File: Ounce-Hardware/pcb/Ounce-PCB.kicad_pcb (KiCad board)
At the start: 2 copper layers, 135 x 61 mm, 5 parts, among them U1 RaspberryPi_Pico2_W, U2 RaspberryPi_Pico, U3 RaspberryPi_Pico, U4 RaspberryPi_Pico, U5 RaspberryPi_Pico

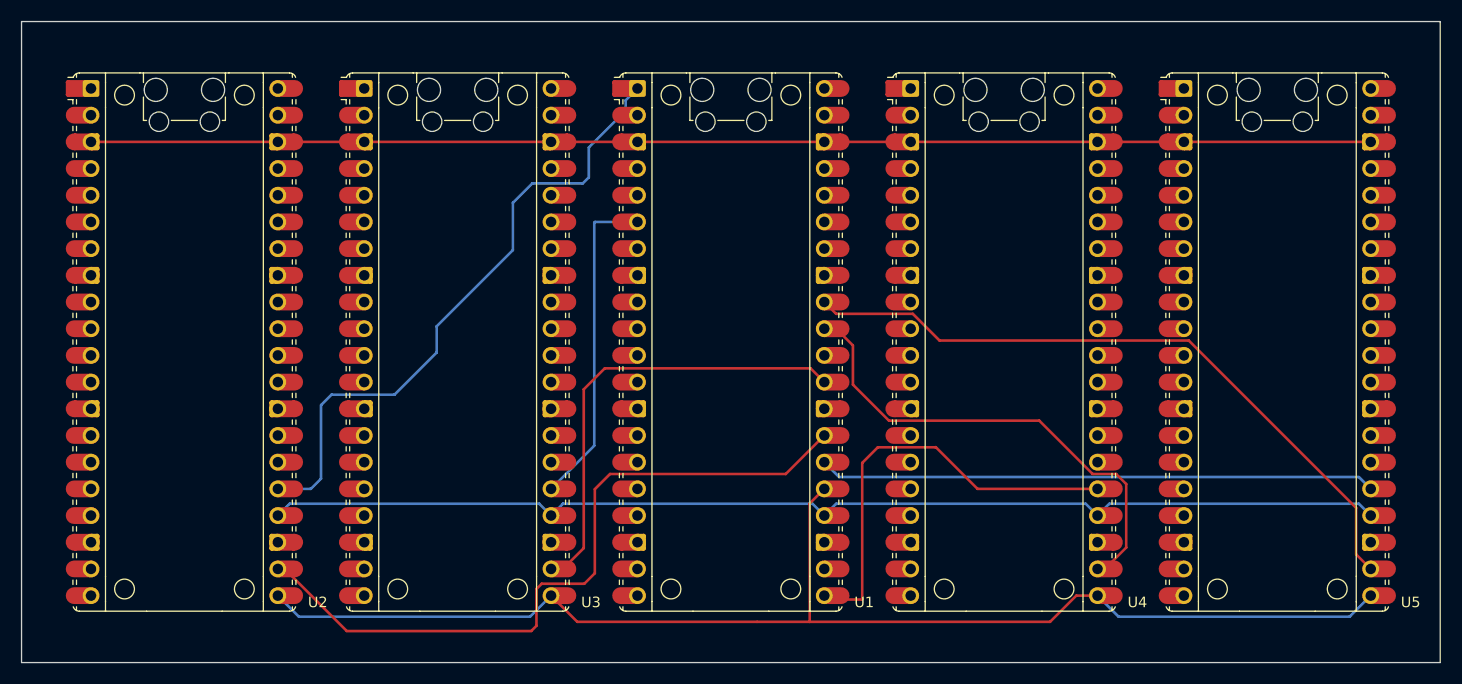
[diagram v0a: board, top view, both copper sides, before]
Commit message: Rotate U1 180 degrees and clear the routing
U1's USB now faces the opposite way to the four servants: rotated 180 degrees
in place at (150,100), still on F.Cu. All 103 track segments removed, so the
board is back to 25 ratlines with nothing routed.

I flipped it to the back first, which was the wrong reading of "flipped" -
that moved the module to B.Cu rather than turning it around. Undone.

The rotation moves U1's inner mounting pads from the top of the module to the
bottom, so the silkscreen no longer fits where it did: the servants are clear
below y=79.95 while U1 is only clear above y=120.05, leaving a common band of
79.95..120.05 instead of the 79.95..124.93 the text was spaced for. Four
silk_over_copper violations showed up where the rows clipped U1's pads.

Rows re-fitted into 81.0..119.0 with an exact 2.167mm gap between each. The
single letters drop from 9mm to 8mm high to make four rows fit that narrower
band without crowding; still the largest text on the board. No silkscreen
violations.

Ground is still restricted to pins 3 and 38.

Co-Authored-By: Claude Opus 5 <noreply@anthropic.com>
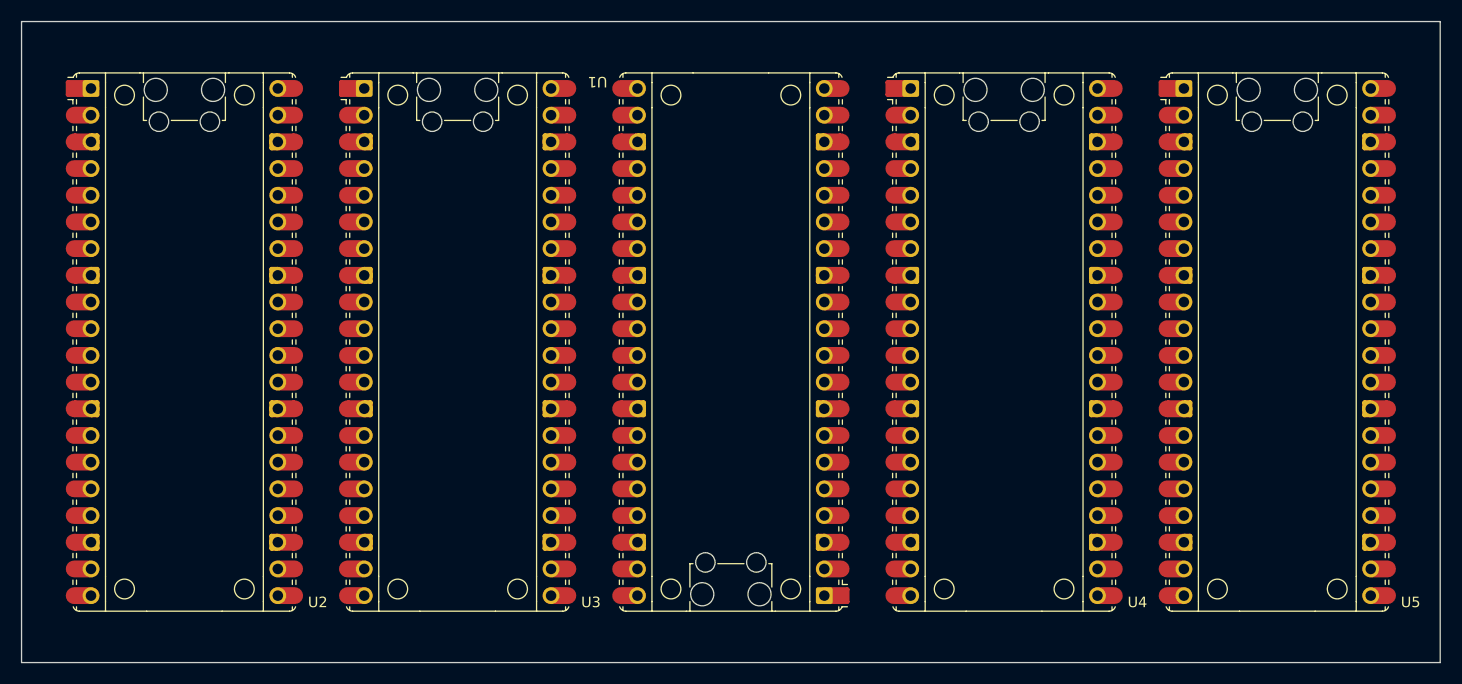
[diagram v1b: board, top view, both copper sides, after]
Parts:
- turned U1 to 180 degrees
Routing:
- net SPI0_MOSI: track 122.6 -> 0.00 mm
- net GND: track 121.8 -> 0.00 mm
- net SPI0_SCK: track 107.7 -> 0.00 mm
- net SPI0_CS0: track 68.9 -> 0.00 mm
- net SPI0_CS3: track 65.1 -> 0.00 mm
- net SPI0_MISO0: track 60.4 -> 0.00 mm
- net SPI0_MISO3: track 53.1 -> 0.00 mm
- net SPI0_CS2: track 46.7 -> 0.00 mm
- net SPI0_CS1: track 43.3 -> 0.00 mm
- net SPI0_MISO2: track 42.3 -> 0.00 mm
- net SPI0_MISO1: track 31.2 -> 0.00 mm

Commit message: Set the display silkscreen in Times New Roman, restore ground
The twelve display texts - OUNCE, THE, TITAN, SLAYER - now use Times New Roman
instead of KiCad's stroke font.

The credit stays in the stroke font, deliberately. At 2mm any TrueType serif
has hairline strokes below the silkscreen minimum, and DRC flags it: Times,
Georgia, Cambria and Palatino all failed at 2.4mm even in bold. It only passes
somewhere above 3.2mm, and by 3.4mm the text is 37.9 x 5.29mm, wider than the
corner allows and taller than the 5.17mm band between the last pad row and the
board edge. That leaves a window too narrow to build on, and hairlines dropping
out is a real silkscreen failure rather than a cosmetic one. The stroke font
has uniform thickness by design and is the right tool at that size.

Ground is restored, but not as it was: the 180 degree rotation moved U1's
ground pins from y=80.95 to y=119.05, so the old straight run no longer reaches
them. The chain now goes along the top through U2 and U3, down the 5mm channel
between U3 and U1 at x=137, across U1 at y=119.05, back up the channel between
U1 and U4 at x=163, then along the top through U4 and U5. Thirteen segments,
198mm, and DRC reports no unconnected ground.

The crossing at y=119.05 clears U1's mounting pads at y=120.05 by 0.88mm.

Co-Authored-By: Claude Opus 5 <noreply@anthropic.com>
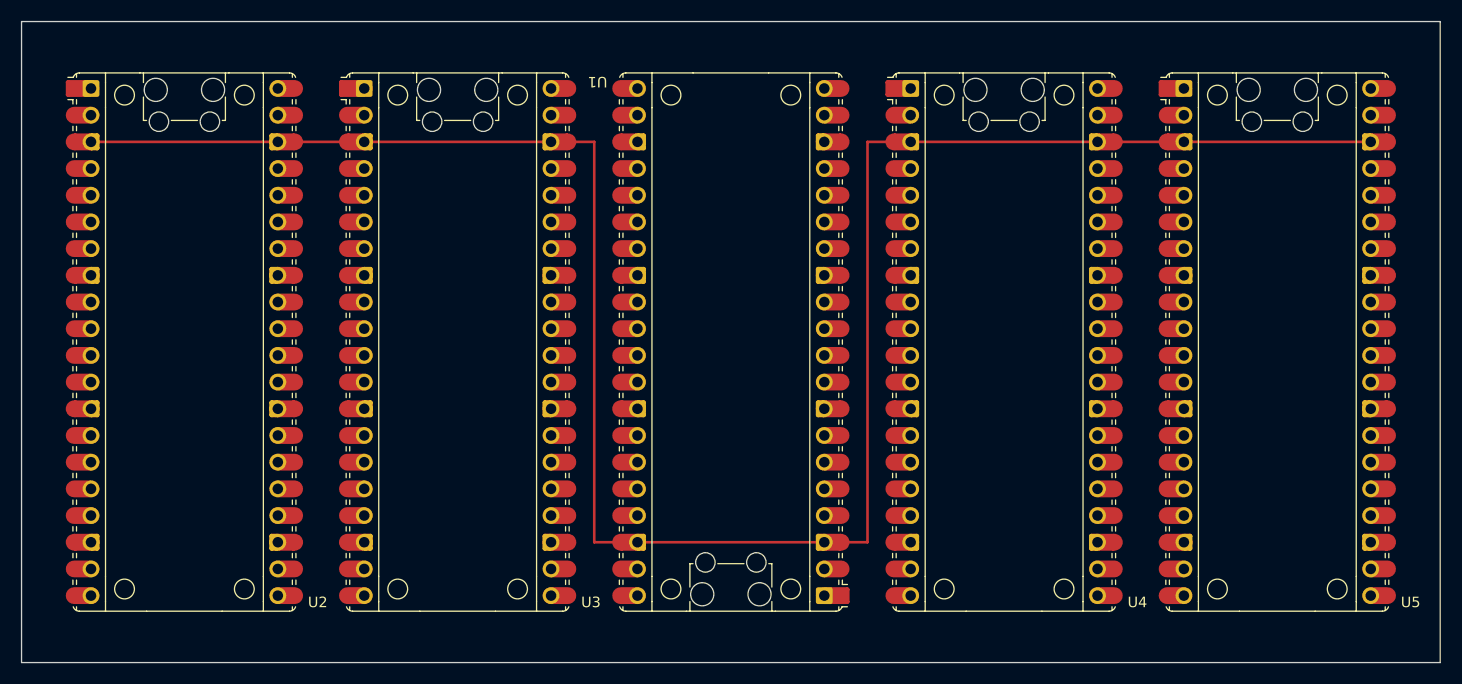
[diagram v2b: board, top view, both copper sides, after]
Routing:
- net GND: track 0.00 -> 198.0 mm
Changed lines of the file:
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@@
 		(effects
 			(font
+				(face "Times New Roman")
 				(size 5.5 2.1)
 				(thickness 0.8)
@@
 		(effects
 			(font
+				(face "Times New Roman")
 				(size 6 4)
 				(thickness 1)
@@
 		(effects
 			(font
+				(face "Times New Roman")
 				(size 8 6.2)
 				(thickness 1.1)
@@
 		(effects
 			(font
+				(face "Times New Roman")
 				(size 8 6.2)
 				(thickness 1.1)
@@
 		(effects
 			(font
+				(face "Times New Roman")
 				(size 8 6.2)
 				(thickness 1.1)
@@
 		(effects
 			(font
+				(face "Times New Roman")
 				(size 8 6.2)
 				(thickness 1.1)
@@
 		(effects
 			(font
+				(face "Times New Roman")
 				(size 8 6.2)
 				(thickness 1.1)
@@
 		(effects
 			(font
+				(face "Times New Roman")
 				(size 8 6.2)
 				(thickness 1.1)
@@
 		(effects
 			(font
+				(face "Times New Roman")
 				(size 8 6.2)
 				(thickness 1.1)
@@
 		(effects
 			(font
+				(face "Times New Roman")
 				(size 8 6.2)
 				(thickness 1.1)
@@
 		(effects
 			(font
+				(face "Times New Roman")
 				(size 8 6.2)
 				(thickness 1.1)
@@
 		(effects
 			(font
-				(size 8 6.2)
-				(thickness 1.1)
-			)
-			(justify mirror)
-		)
+				(face "Times New Roman")
+				(size 8 6.2)
+				(thickness 1.1)
+			)
+			(justify mirror)
+		)
+	)
+	(segment
+		(start 115.11 80.95)
+		(end 132.889999 80.95)
+		(width 0.25)
+		(layer "F.Cu")
+		(net "GND")
+	)
+	(segment
+		(start 163 119.05)
+		(end 163 80.95)
+		(width 0.25)
+		(layer "F.Cu")
+		(net "GND")
+	)
+	(segment
+		(start 167.11 80.95)
+		(end 184.89 80.95)
+		(width 0.25)
+		(layer "F.Cu")
+		(net "GND")
+	)
+	(segment
+		(start 184.89 80.95)
+		(end 193.11 80.95)
+		(width 0.25)
+		(layer "F.Cu")
+		(net "GND")
+	)
+	(segment
+		(start 163 80.95)
+		(end 167.11 80.95)
+		(width 0.25)
+		(layer "F.Cu")
+		(net "GND")
+	)
+	(segment
+		(start 141.11 119.05)
+		(end 158.89 119.05)
+		(width 0.25)
+		(layer "F.Cu")
+		(net "GND")
+	)
+	(segment
+		(start 132.889999 80.95)
+		(end 137 80.95)
+		(width 0.25)
+		(layer "F.Cu")
+		(net "GND")
+	)
+	(segment
+		(start 193.11 80.95)
+		(end 210.89 80.95)
+		(width 0.25)
+		(layer "F.Cu")
+		(net "GND")
+	)
+	(segment
+		(start 137 119.05)
+		(end 141.11 119.05)
+		(width 0.25)
+		(layer "F.Cu")
+		(net "GND")
+	)
+	(segment
+		(start 158.89 119.05)
+		(end 163 119.05)
+		(width 0.25)
+		(layer "F.Cu")
+		(net "GND")
+	)
+	(segment
+		(start 137 80.95)
+		(end 137 119.05)
+		(width 0.25)
+		(layer "F.Cu")
+		(net "GND")
+	)
+	(segment
+		(start 106.89 80.95)
+		(end 115.11 80.95)
+		(width 0.25)
+		(layer "F.Cu")
+		(net "GND")
+	)
+	(segment
+		(start 89.11 80.95)
+		(end 106.89 80.95)
+		(width 0.25)
+		(layer "F.Cu")
+		(net "GND")
 	)
 	(embedded_fonts no)

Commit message: Clear the generated ground routing
Removes the 13 GND segments from the previous commit, leaving the board with no
tracks at all so the ground can be laid out by hand alongside the signals.

Back to 25 unconnected: 16 signal and 9 ground.

Co-Authored-By: Claude Opus 5 <noreply@anthropic.com>
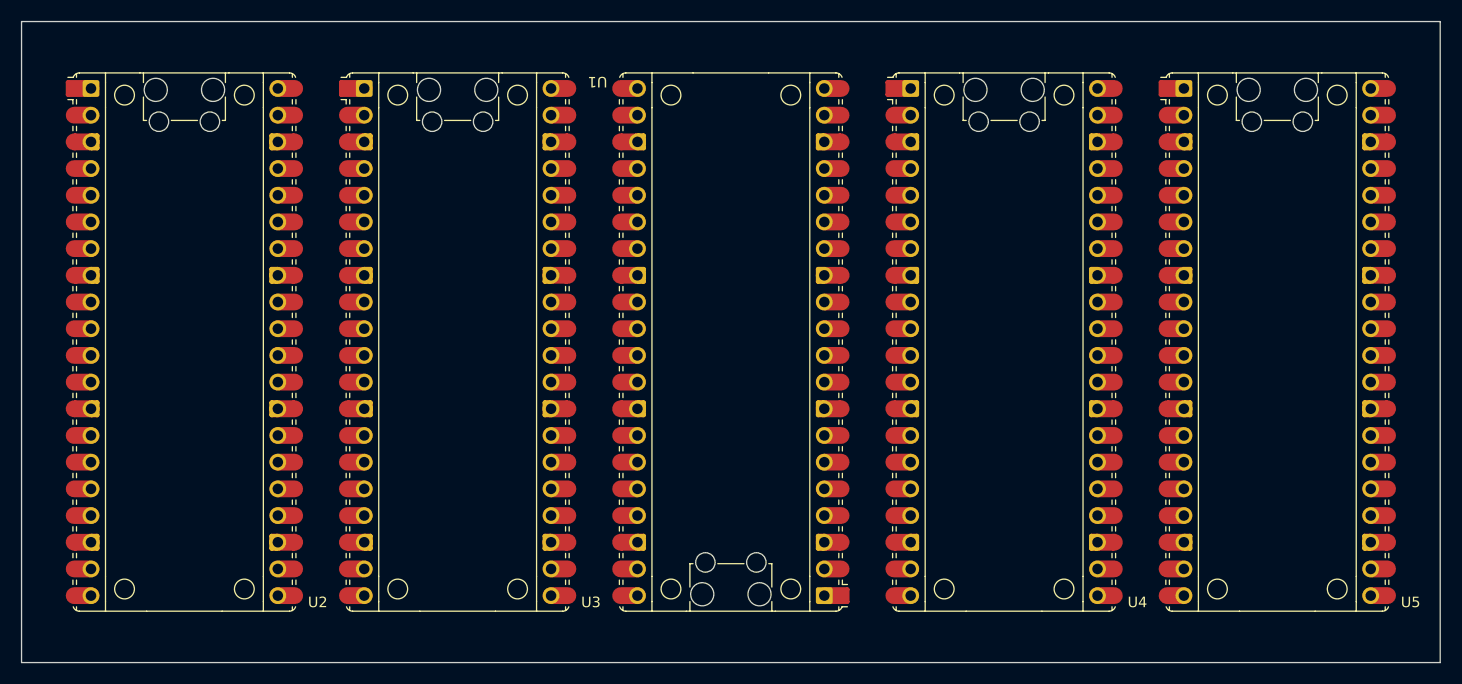
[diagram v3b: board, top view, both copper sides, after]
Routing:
- net GND: track 198.0 -> 0.00 mm

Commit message: Remove a duplicate via on SPI0_CS2
Two vias were stacked at exactly (170.500, 108.500), same net, same drill -
DRC's holes_co_located. One is redundant and would have the fab drill the same
hole twice. Dropped one; connectivity is unchanged since the remaining via
holds the same layer transition.

Board now: all ten signal nets routed and matching spi_master.cpp, 960mm of
copper across 6 vias. The only unconnected items left are ground.

Co-Authored-By: Claude Opus 5 <noreply@anthropic.com>
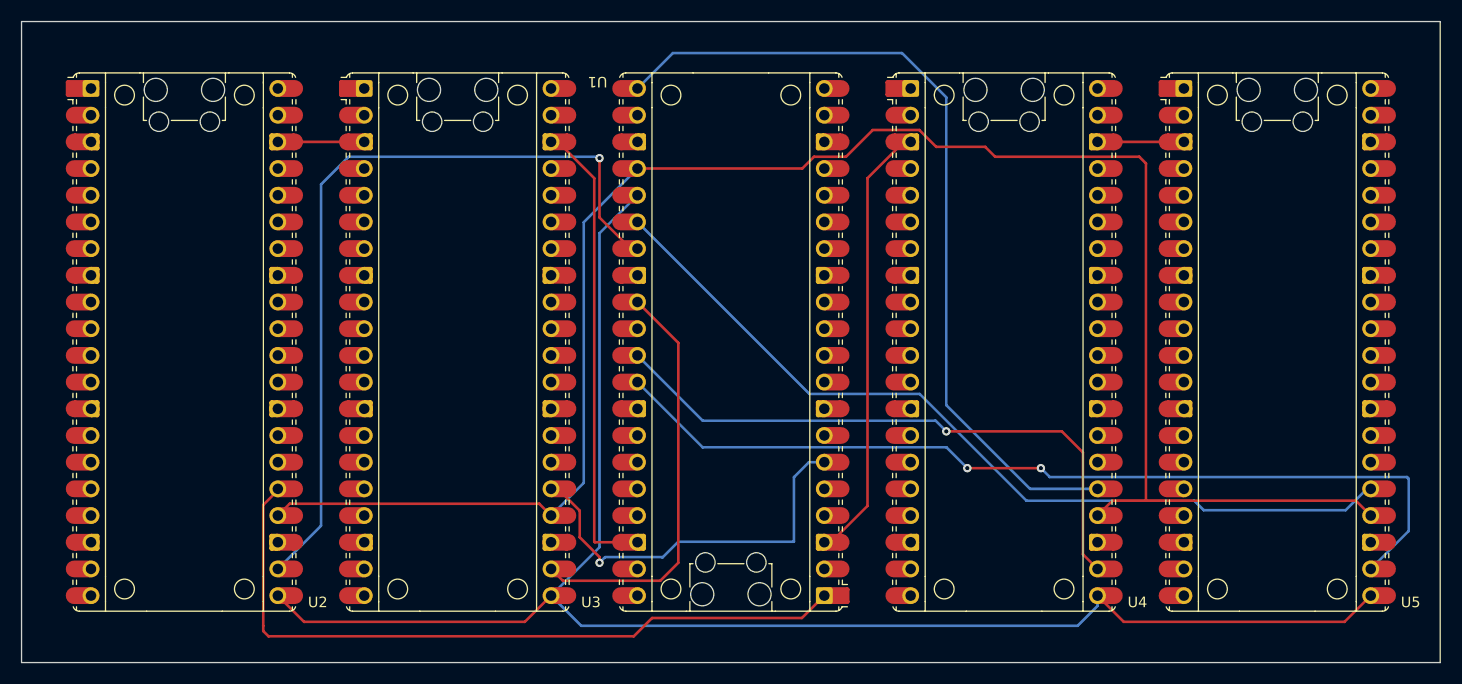
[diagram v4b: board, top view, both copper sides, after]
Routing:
- net SPI0_SCK: track 0.00 -> 173.9 mm
- net SPI0_MOSI: track 0.00 -> 152.6 mm
- net GND: track 0.00 -> 103.0 mm
- net SPI0_CS3: track 0.00 -> 87.3 mm, vias 0 -> 2
- net SPI0_MISO3: track 0.00 -> 82.0 mm
- net SPI0_MISO2: track 0.00 -> 79.5 mm
- net SPI0_CS0: track 0.00 -> 76.4 mm, vias 0 -> 1
- net SPI0_MISO0: track 0.00 -> 69.3 mm
- net SPI0_CS2: track 0.00 -> 57.9 mm, vias 0 -> 1
- net SPI0_CS1: track 0.00 -> 39.7 mm
- net SPI0_MISO1: track 0.00 -> 38.3 mm, vias 0 -> 1

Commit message: Extend the ground routing
Ground goes from 12 segments to 23, 103mm to 188mm. Copper networks drop from
four islands plus two orphans to two islands plus two orphans, and DRC
unconnected from 5 to 3.

U3 and U4 no longer bridge internally - both now have copper from pin 3 to pin
38. The left half (U2, U3) and right half (U4, U5) are each solid, and the only
remaining internal dependency is U1.

Co-Authored-By: Claude Opus 5 <noreply@anthropic.com>
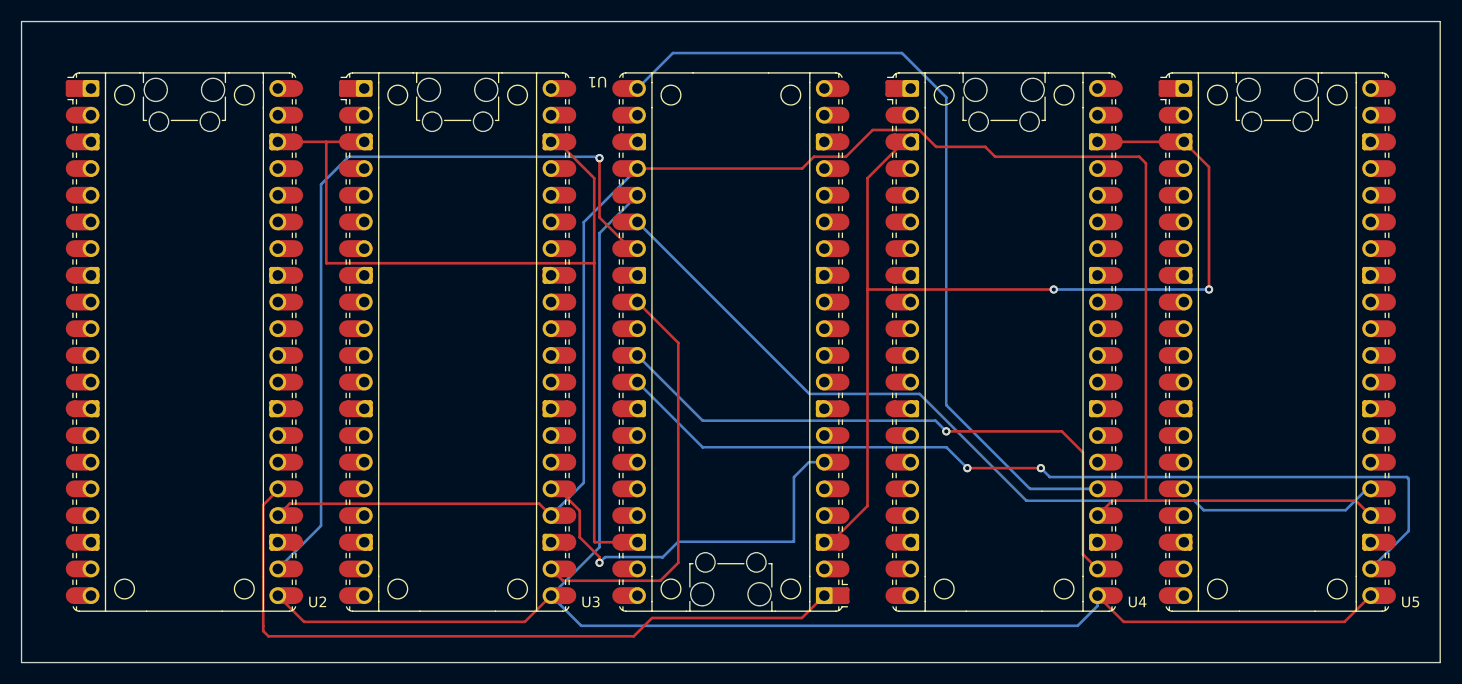
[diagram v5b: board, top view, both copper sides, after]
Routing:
- net GND: track 103.0 -> 187.6 mm, vias 0 -> 2
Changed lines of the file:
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@@
 	)
 	(segment
-		(start 137 119)
+		(start 137 92.5)
 		(end 137 84.40901)
+		(width 0.25)
+		(layer "F.Cu")
+		(net "GND")
+	)
+	(segment
+		(start 111.5 80.95)
+		(end 111.5 92.5)
+		(width 0.25)
+		(layer "F.Cu")
+		(net "GND")
+	)
+	(segment
+		(start 111.5 92.5)
+		(end 137 92.5)
+		(width 0.25)
+		(layer "F.Cu")
+		(net "GND")
+	)
+	(segment
+		(start 193.11 80.95)
+		(end 195.5 83.34)
 		(width 0.25)
 		(layer "F.Cu")
@@
 	)
 	(segment
+		(start 106.89 80.95)
+		(end 111.5 80.95)
+		(width 0.25)
+		(layer "F.Cu")
+		(net "GND")
+	)
+	(segment
 		(start 166.45901 80.95)
 		(end 163 84.40901)
@@
 		(start 133.54099 80.95)
 		(end 132.89 80.95)
+		(width 0.25)
+		(layer "F.Cu")
+		(net "GND")
+	)
+	(segment
+		(start 137 119)
+		(end 137 92.5)
+		(width 0.25)
+		(layer "F.Cu")
+		(net "GND")
+	)
+	(segment
+		(start 163 95)
+		(end 163 115.59099)
 		(width 0.25)
 		(layer "F.Cu")
@@
 	)
 	(segment
+		(start 180.725 95)
+		(end 163 95)
+		(width 0.25)
+		(layer "F.Cu")
+		(net "GND")
+	)
+	(segment
 		(start 163 115.59099)
 		(end 159.54099 119.05)
@@
 	)
 	(segment
-		(start 106.89 80.95)
+		(start 111.5 80.95)
 		(end 115.11 80.95)
 		(width 0.25)
@@
 	)
 	(segment
-		(start 163 84.40901)
-		(end 163 115.59099)
+		(start 195.5 83.34)
+		(end 195.5 95)
 		(width 0.25)
 		(layer "F.Cu")
 		(net "GND")
 	)
+	(segment
+		(start 163 84.40901)
+		(end 163 95)
+		(width 0.25)
+		(layer "F.Cu")
+		(net "GND")
+	)
+	(via
+		(at 180.725 95)
+		(size 0.8)
+		(drill 0.4)
+		(layers "F.Cu" "B.Cu")
+		(net "GND")
+	)
+	(via
+		(at 195.5 95)
+		(size 0.8)
+		(drill 0.4)
+		(layers "F.Cu" "B.Cu")
+		(net "GND")
+	)
+	(segment
+		(start 195.5 95)
+		(end 180.725 95)
+		(width 0.25)
+		(layer "B.Cu")
+		(net "GND")
+	)
